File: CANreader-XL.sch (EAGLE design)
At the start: 101 parts, among them IC1 STM32F107RBT, IC2 TJA1055T/3, IC3 BD9G101G, IC4 LM1117IMPX-3.3, IC5 MCP2562-SOIC8, IC7 DP83848I, Q1 25MHz, SW1 SLEEP, SW2 TERM, U1 HC_05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

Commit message: Attrmpt to route
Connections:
- removed net N$30: J1.P5
- net +3V3: now also J1.P4, J1.P5
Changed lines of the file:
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@@
 </segment>
 <segment>
-<wire x1="190.5" y1="-106.68" x2="190.5" y2="-73.66" width="0.1524" layer="91"/>
+<wire x1="190.5" y1="-119.38" x2="190.5" y2="-73.66" width="0.1524" layer="91"/>
 <pinref part="+3V21" gate="G$1" pin="+3V3"/>
 <pinref part="C39" gate="G$1" pin="1"/>
@@
 <wire x1="195.58" y1="-76.2" x2="195.58" y2="-73.66" width="0.1524" layer="91"/>
 <junction x="195.58" y="-73.66"/>
+<pinref part="J1" gate="G$1" pin="P5"/>
+<wire x1="203.2" y1="-119.38" x2="190.5" y2="-119.38" width="0.1524" layer="91"/>
+<pinref part="J1" gate="G$1" pin="P4"/>
+<wire x1="203.2" y1="-121.92" x2="190.5" y2="-121.92" width="0.1524" layer="91"/>
+<wire x1="190.5" y1="-121.92" x2="190.5" y2="-119.38" width="0.1524" layer="91"/>
+<junction x="190.5" y="-119.38"/>
 </segment>
 <segment>
@@
 </segment>
 </net>
-<net name="N$30" class="0">
-<segment>
-<pinref part="J1" gate="G$1" pin="P5"/>
-<wire x1="203.2" y1="-119.38" x2="190.5" y2="-119.38" width="0.1524" layer="91"/>
-<wire x1="190.5" y1="-119.38" x2="190.5" y2="-106.68" width="0.1524" layer="91"/>
-</segment>
-</net>

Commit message: Route attempt
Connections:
- net HC_KEY: now also IC1MCU.PA8; no longer IC1MCU.PA15
- net N$6: now also IC1MCU.PB14; no longer IC1MCU.PA8
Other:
- moved on the sheet: LED1, R21
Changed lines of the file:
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@@
 <instance part="+3V3" gate="G$1" x="175.26" y="147.32" rot="R90"/>
 <instance part="+3V9" gate="G$1" x="-33.02" y="10.16"/>
-<instance part="R21" gate="G$1" x="139.7" y="17.78"/>
-<instance part="GND30" gate="1" x="157.48" y="12.7"/>
+<instance part="R21" gate="G$1" x="137.16" y="76.2"/>
+<instance part="GND30" gate="1" x="154.94" y="71.12"/>
 <instance part="+3V10" gate="G$1" x="53.34" y="-35.56"/>
 <instance part="GND2" gate="1" x="33.02" y="-83.82"/>
@@
 <instance part="LED2" gate="G$1" x="266.7" y="-30.48"/>
 <instance part="LED3" gate="G$1" x="256.54" y="-30.48"/>
-<instance part="LED1" gate="G$1" x="149.86" y="17.78" rot="R90"/>
+<instance part="LED1" gate="G$1" x="147.32" y="76.2" rot="R90"/>
 <instance part="SW2" gate="G$1" x="-55.88" y="-104.14"/>
 <instance part="SW1" gate="G$1" x="228.6" y="132.08"/>
@@
 <pinref part="GND30" gate="1" pin="GND"/>
 <pinref part="LED1" gate="G$1" pin="C"/>
-<wire x1="154.94" y1="17.78" x2="157.48" y2="17.78" width="0.1524" layer="91"/>
-<wire x1="157.48" y1="17.78" x2="157.48" y2="15.24" width="0.1524" layer="91"/>
+<wire x1="152.4" y1="76.2" x2="154.94" y2="76.2" width="0.1524" layer="91"/>
+<wire x1="154.94" y1="76.2" x2="154.94" y2="73.66" width="0.1524" layer="91"/>
 </segment>
 <segment>
@@
 </segment>
 <segment>
-<label x="99.06" y="35.56" size="1.778" layer="95" xref="yes"/>
-<wire x1="99.06" y1="35.56" x2="96.52" y2="35.56" width="0.1524" layer="91"/>
-<pinref part="IC1" gate="MCU" pin="PA15"/>
+<label x="121.92" y="17.78" size="1.778" layer="95" xref="yes"/>
+<pinref part="IC1" gate="MCU" pin="PA8"/>
+<wire x1="96.52" y1="17.78" x2="121.92" y2="17.78" width="0.1524" layer="91"/>
 </segment>
 </net>
@@
 <segment>
 <pinref part="R21" gate="G$1" pin="2"/>
-<wire x1="144.78" y1="17.78" x2="147.32" y2="17.78" width="0.1524" layer="91"/>
+<wire x1="142.24" y1="76.2" x2="144.78" y2="76.2" width="0.1524" layer="91"/>
 <pinref part="LED1" gate="G$1" pin="A"/>
 </segment>
@@
 <net name="N$6" class="0">
 <segment>
-<pinref part="IC1" gate="MCU" pin="PA8"/>
 <pinref part="R21" gate="G$1" pin="1"/>
-<wire x1="96.52" y1="17.78" x2="134.62" y2="17.78" width="0.1524" layer="91"/>
-</segment>
-</net>
+<pinref part="IC1" gate="MCU" pin="PB14"/>
+<wire x1="96.52" y1="76.2" x2="132.08" y2="76.2" width="0.1524" layer="91"/>
+</segment>
+</net>

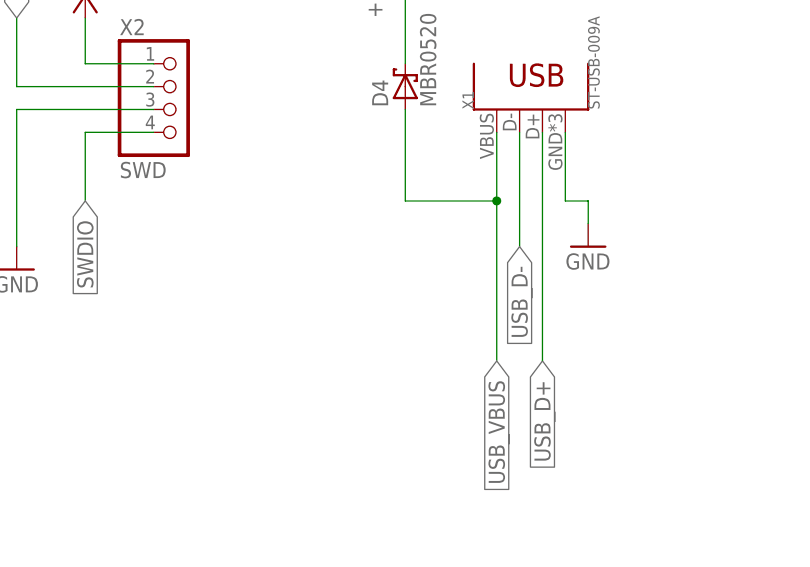
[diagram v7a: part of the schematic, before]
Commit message: USB VDD capacitor
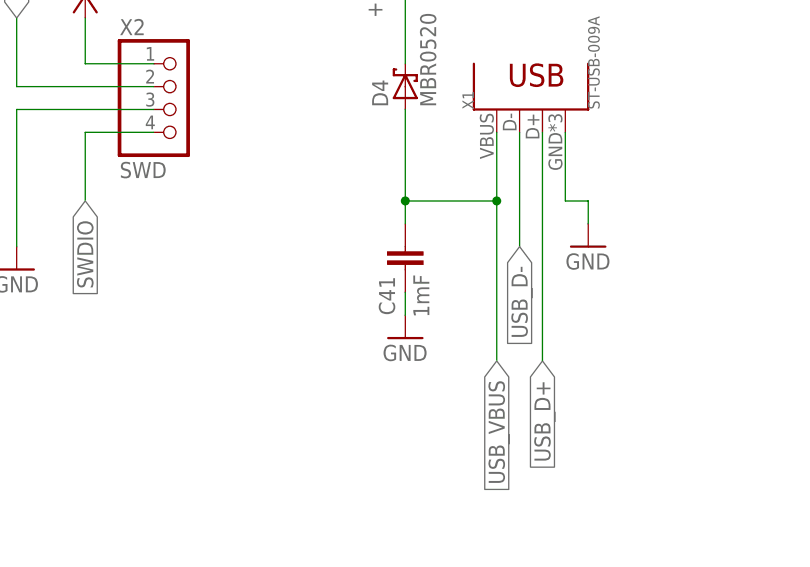
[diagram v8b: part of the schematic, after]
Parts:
- added C41: 1mF, rcl:C-EUC0805
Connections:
- net GND: now also C41.2
- net USB_VBUS: now also C41.1
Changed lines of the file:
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@@
 <part name="R6" library="rcl" deviceset="R-EU_" device="R0805" value="10K"/>
 <part name="R9" library="rcl" deviceset="R-EU_" device="R0805" value="470"/>
+<part name="C41" library="rcl" deviceset="C-EU" device="C0805" value="1mF"/>
+<part name="GND24" library="supply1" deviceset="GND" device=""/>
 </parts>
 <sheets>
@@
 <instance part="R6" gate="G$1" x="17.78" y="-2.54"/>
 <instance part="R9" gate="G$1" x="248.92" y="-25.4"/>
+<instance part="C41" gate="G$1" x="-40.64" y="53.34" smashed="yes">
+<attribute name="NAME" x="-43.561" y="50.038" size="1.778" layer="95" rot="R270"/>
+<attribute name="VALUE" x="-37.973" y="45.466" size="1.778" layer="96" rot="R90"/>
+</instance>
+<instance part="GND24" gate="1" x="-40.64" y="43.18"/>
 </instances>
 <busses>
@@
 <pinref part="GND12" gate="1" pin="GND"/>
 <wire x1="-12.7" y1="-68.58" x2="-12.7" y2="-71.12" width="0.1524" layer="91"/>
+</segment>
+<segment>
+<pinref part="GND24" gate="1" pin="GND"/>
+<pinref part="C41" gate="G$1" pin="2"/>
+<wire x1="-40.64" y1="45.72" x2="-40.64" y2="48.26" width="0.1524" layer="91"/>
 </segment>
 </net>
@@
 <label x="-30.48" y="40.64" size="1.778" layer="95" rot="R270" xref="yes"/>
 <pinref part="X1" gate="G$1" pin="1"/>
-</segment>
-</net>
+<pinref part="C41" gate="G$1" pin="1"/>
+<wire x1="-40.64" y1="55.88" x2="-40.64" y2="58.42" width="0.1524" layer="91"/>
+<junction x="-40.64" y="58.42"/>
+</segment>
+</net>
